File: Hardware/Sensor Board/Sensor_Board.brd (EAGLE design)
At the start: 100 x 80 mm, 15 parts, among them U1 ATMEGA328P_PDIP

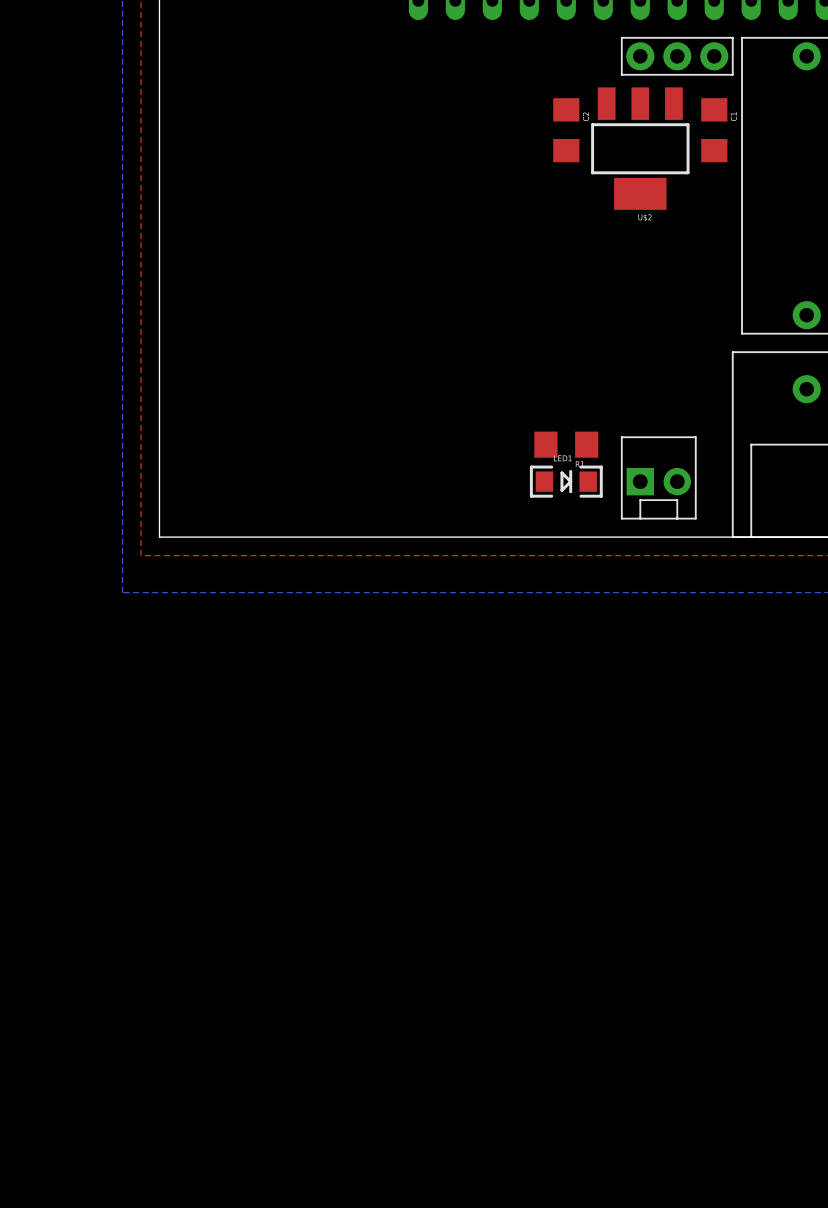
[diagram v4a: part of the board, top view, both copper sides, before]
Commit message: Reorganize Schematic
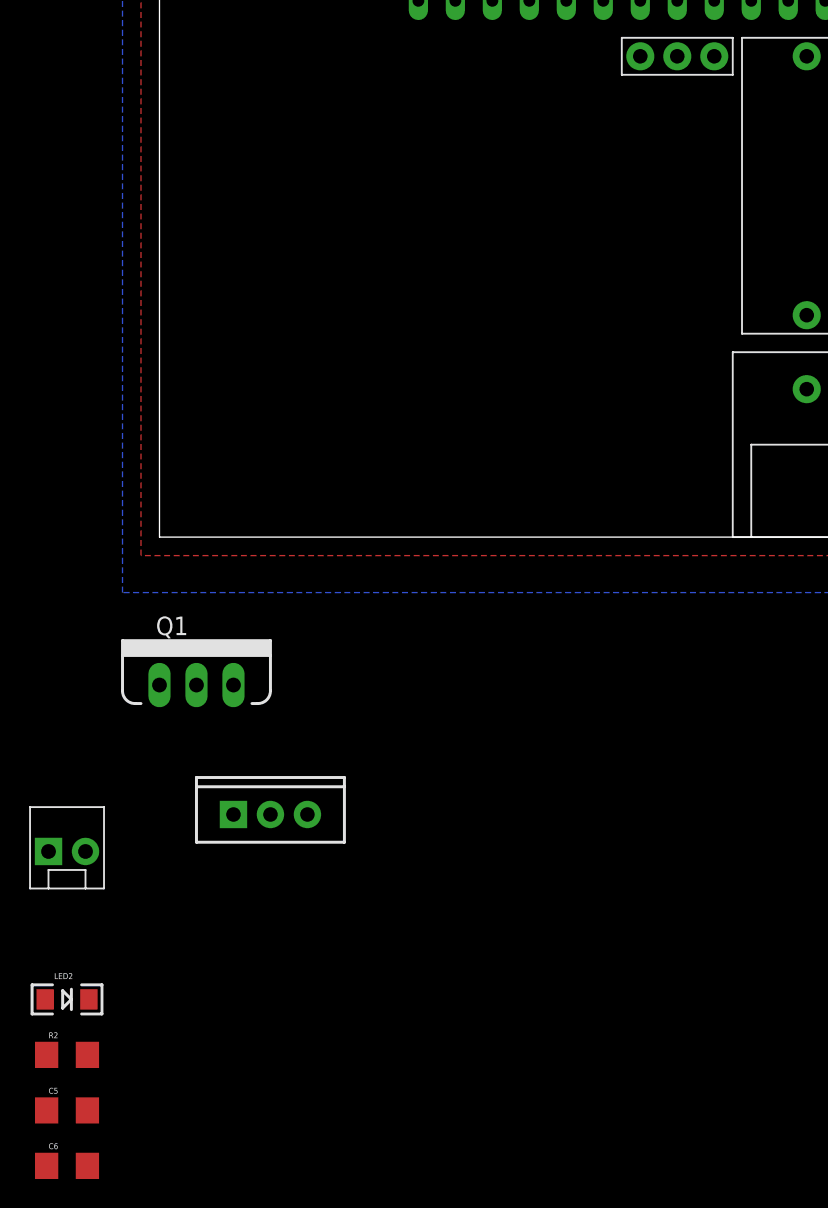
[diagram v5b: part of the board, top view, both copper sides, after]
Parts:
- removed C1, C2: .1uF, SparkFun-Passives:1206
- removed JP2: M02POLAR, SparkFun-Connectors:MOLEX-1X2
- removed LED1: (no value), SparkFun-LED:LED-1206
- removed R1: 1k, SparkFun-Passives:1206
- removed U$2: V_REG_LM3940, SparkFun-PowerIC:SOT223
- added C5: 100uF, SparkFun-Capacitors:1206
- added C6: 10uF, SparkFun-Capacitors:1206
- added IC1: (no value), SparkFun-PowerIC:TO220-IGO
- added JP1: M02POLAR, SparkFun-Connectors:MOLEX-1X2
- added LED2: (no value), SparkFun-LED:LED-1206
- added Q1: MOSFET-NCHANNELFQP30N06L, SparkFun-DiscreteSemi:TO220V
- added R2: 1k, SparkFun-Passives:1206
- C3, C4: value (none) -> 22pF
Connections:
- net RX renamed PH_SENS_RX
- net TO_LAZER renamed 3V3_LASER
- net TX renamed PH_SENS_TX
- removed net N$8: LED1.A, R1.2
- removed net TO_MOSFET: JP3.1
- new net 12V: C5.1, IC1.IN, JP1.2
- new net N$1: JP3.1, Q1.2
- new net N$3: LED2.C, R2.1
- net 3.3V: no longer C2.1, U$2.3
- net 5V: now also C6.1, IC1.OUT, LED2.A; no longer C1.1, JP2.2, R1.1, U$2.1
- net GND: now also C5.2, C6.2, IC1.GND, JP1.1, R2.2; no longer C1.2, C2.2, JP2.1, LED1.C, U$2.2
- net LASER_CTR: now also Q1.1
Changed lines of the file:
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@@
 </autorouter>
 <elements>
-<element name="JP2" library="SparkFun-Connectors" package="MOLEX-1X2" value="M02POLAR" x="33.02" y="3.81"/>
 <element name="JP3" library="SparkFun-Connectors" package="MOLEX-1X2" value="M02POLAR" x="16.51" y="49.53" rot="R180"/>
-<element name="U$2" library="SparkFun-PowerIC" package="SOT223" value="V_REG_LM3940" x="33.02" y="26.67" rot="R180"/>
-<element name="C1" library="SparkFun-Passives" package="1206" value=".1uF" x="38.1" y="27.94" rot="R270"/>
-<element name="C2" library="SparkFun-Passives" package="1206" value=".1uF" x="27.94" y="27.94" rot="R270"/>
-<element name="LED1" library="SparkFun-LED" package="LED-1206" value="" x="27.94" y="3.81"/>
-<element name="R1" library="SparkFun-Passives" package="1206" value="1k" x="27.94" y="6.35" rot="R180"/>
 <element name="U$3" library="pH_EZ0" package="PH_EZ0" value="PH_EZ0" x="40.005" y="13.97"/>
 <element name="U$4" library="PH_CONNECTOR" package="PH_CONNECTOR" value="PH_CONNECTOR" x="46.99" y="7.62"/>
@@
 <element name="U1" library="SparkFun-DigitalIC" package="DIL28-3" value="ATMEGA328P_PDIP" x="34.29" y="40.64" rot="R180"/>
 <element name="U$5" library="moisture sensor" package="MOISTURE_SENSOR" value="MOISTURE_SENSOR" x="35.56" y="33.02"/>
-<element name="C3" library="SparkFun-Passives" package="1206" value="" x="29.21" y="46.99"/>
-<element name="C4" library="SparkFun-Passives" package="1206" value="" x="22.86" y="46.99" rot="R180"/>
+<element name="C3" library="SparkFun-Passives" package="1206" value="22pF" x="29.21" y="46.99"/>
+<element name="C4" library="SparkFun-Passives" package="1206" value="22pF" x="22.86" y="46.99" rot="R180"/>
 <element name="U$6" library="CCD_CONNECTOR" package="CCD_CONNECTOR" value="CCD_CONNECTOR" x="38.1" y="48.26" rot="R180"/>
+<element name="Q1" library="SparkFun-DiscreteSemi" package="TO220V" value="MOSFET-NCHANNELFQP30N06L" x="2.54" y="-10.16">
+<attribute name="PROD_ID" value="TRANS-10060" x="2.54" y="-10.16" size="1.778" layer="27" display="off"/>
+</element>
+<element name="IC1" library="SparkFun-PowerIC" package="TO220-IGO" value="" x="7.62" y="-19.05"/>
+<element name="JP1" library="SparkFun-Connectors" package="MOLEX-1X2" value="M02POLAR" x="-7.62" y="-21.59"/>
+<element name="LED2" library="SparkFun-LED" package="LED-1206" value="" x="-6.35" y="-31.75"/>
+<element name="R2" library="SparkFun-Passives" package="1206" value="1k" x="-6.35" y="-35.56"/>
+<element name="C5" library="SparkFun-Capacitors" package="1206" value="100uF" x="-6.35" y="-39.37"/>
+<element name="C6" library="SparkFun-Capacitors" package="1206" value="10uF" x="-6.35" y="-43.18"/>
 </elements>
 <signals>
 <signal name="GND">
-<contactref element="JP2" pad="1"/>
-<contactref element="C1" pad="2"/>
-<contactref element="U$2" pad="2"/>
-<contactref element="C2" pad="2"/>
-<contactref element="LED1" pad="C"/>
 <contactref element="U$3" pad="GND"/>
-<contactref element="U$3" pad="PGND"/>
-<contactref element="U$4" pad="GND"/>
 <contactref element="U1" pad="22"/>
 <contactref element="U1" pad="8"/>
@@
 <contactref element="C3" pad="2"/>
 <contactref element="U$6" pad="GND"/>
+<contactref element="IC1" pad="GND"/>
+<contactref element="JP1" pad="1"/>
+<contactref element="R2" pad="2"/>
+<contactref element="C5" pad="2"/>
+<contactref element="C6" pad="2"/>
+<contactref element="U$3" pad="PGND"/>
+<contactref element="U$4" pad="GND"/>
 <wire x1="33.02" y1="44.45" x2="30.61" y2="46.99" width="0" layer="19" extent="1-1"/>
-<wire x1="33.02" y1="29.7688" x2="33.02" y2="33.02" width="0" layer="19" extent="1-1"/>
-<wire x1="29.44" y1="3.81" x2="33.02" y2="3.81" width="0" layer="19" extent="1-1"/>
-<wire x1="38.1" y1="26.54" x2="33.02" y2="29.7688" width="0" layer="19" extent="1-1"/>
-<wire x1="27.94" y1="26.54" x2="33.02" y2="29.7688" width="0" layer="19" extent="1-1"/>
 <wire x1="21.46" y1="46.99" x2="30.61" y2="46.99" width="0" layer="19" extent="1-1"/>
+<wire x1="7.62" y1="-19.05" x2="49.53" y2="10.16" width="0" layer="19" extent="1-1"/>
+<wire x1="-7.62" y1="-21.59" x2="7.62" y2="-19.05" width="0" layer="19" extent="1-1"/>
+<wire x1="-4.95" y1="-35.56" x2="-7.62" y2="-21.59" width="0" layer="19" extent="1-1"/>
+<wire x1="-4.95" y1="-39.37" x2="-4.95" y2="-35.56" width="0" layer="19" extent="1-1"/>
+<wire x1="-4.95" y1="-43.18" x2="-4.95" y2="-39.37" width="0" layer="19" extent="1-1"/>
 </signal>
 <signal name="5V">
-<contactref element="JP2" pad="2"/>
-<contactref element="U$2" pad="1"/>
-<contactref element="C1" pad="1"/>
-<contactref element="R1" pad="1"/>
-<contactref element="U$3" pad="VCC"/>
-<contactref element="U$4" pad="VCC"/>
 <contactref element="U$5" pad="VCC"/>
 <polygon width="0.4064" layer="1">
@@
 </polygon>
 <contactref element="U$6" pad="5V"/>
+<contactref element="IC1" pad="OUT"/>
+<contactref element="LED2" pad="A"/>
+<contactref element="C6" pad="1"/>
+<contactref element="U$3" pad="VCC"/>
+<contactref element="U$4" pad="VCC"/>
+<wire x1="-7.85" y1="-31.75" x2="-7.75" y2="-43.18" width="0" layer="19" extent="1-1"/>
+<wire x1="10.16" y1="-19.05" x2="-7.85" y2="-31.75" width="0" layer="19" extent="1-1"/>
+<wire x1="44.45" y1="10.16" x2="10.16" y2="-19.05" width="0" layer="19" extent="1-1"/>
 </signal>
 <signal name="3.3V">
-<contactref element="C2" pad="1"/>
-<contactref element="U$2" pad="3"/>
 <contactref element="U1" pad="7"/>
 <contactref element="U1" pad="21"/>
@@
 <wire x1="33.02" y1="36.83" x2="35.56" y2="44.45" width="0" layer="19" extent="1-1"/>
 <wire x1="30.48" y1="36.83" x2="33.02" y2="36.83" width="0" layer="19" extent="1-1"/>
-<wire x1="30.7086" y1="29.7688" x2="30.48" y2="36.83" width="0" layer="19" extent="1-1"/>
-<wire x1="27.94" y1="29.34" x2="30.7086" y2="29.7688" width="0" layer="19" extent="1-1"/>
-</signal>
-<signal name="N$8">
-<contactref element="R1" pad="2"/>
-<contactref element="LED1" pad="A"/>
-<wire x1="26.44" y1="3.81" x2="26.54" y2="6.35" width="0" layer="19" extent="1-1"/>
-</signal>
-<signal name="RX">
-<contactref element="U$3" pad="RX"/>
-<contactref element="U1" pad="4"/>
-<wire x1="49.53" y1="33.02" x2="43.18" y2="44.45" width="0" layer="19" extent="1-1"/>
 </signal>
 <signal name="N$5">
@@
 <wire x1="24.26" y1="46.99" x2="22.86" y2="50.8" width="0" layer="19" extent="1-1"/>
 <wire x1="27.94" y1="44.45" x2="24.26" y2="46.99" width="0" layer="19" extent="1-1"/>
-</signal>
-<signal name="TX">
-<contactref element="U$3" pad="TX"/>
-<contactref element="U1" pad="5"/>
-<wire x1="46.99" y1="33.02" x2="40.64" y2="44.45" width="0" layer="19" extent="1-1"/>
 </signal>
 <signal name="MOIS_SENSOR">
@@
 <signal name="LASER_CTR">
 <contactref element="U1" pad="12"/>
+<contactref element="Q1" pad="1"/>
+<wire x1="0" y1="-10.16" x2="22.86" y2="44.45" width="0" layer="19" extent="1-1"/>
 </signal>
-<signal name="TO_LAZER">
+<signal name="3V3_LASER">
 <contactref element="JP3" pad="2"/>
-</signal>
-<signal name="TO_MOSFET">
-<contactref element="JP3" pad="1"/>
 </signal>
 <signal name="N$2">
@@
 <wire x1="30.48" y1="44.45" x2="27.81" y2="46.99" width="0" layer="19" extent="1-1"/>
 </signal>
+<signal name="N$1">
+<contactref element="JP3" pad="1"/>
+<contactref element="Q1" pad="2"/>
+<wire x1="2.54" y1="-10.16" x2="16.51" y2="49.53" width="0" layer="19" extent="1-1"/>
+</signal>
+<signal name="PH_SENS_RX">
+<contactref element="U1" pad="4"/>
+<contactref element="U$3" pad="RX"/>
+<wire x1="49.53" y1="33.02" x2="43.18" y2="44.45" width="0" layer="19" extent="1-1"/>
+</signal>
+<signal name="PH_SENS_TX">
+<contactref element="U1" pad="5"/>
+<contactref element="U$3" pad="TX"/>
+<wire x1="46.99" y1="33.02" x2="40.64" y2="44.45" width="0" layer="19" extent="1-1"/>
+</signal>
+<signal name="12V">
+<contactref element="JP1" pad="2"/>
+<contactref element="IC1" pad="IN"/>
+<contactref element="C5" pad="1"/>
+<wire x1="-5.08" y1="-21.59" x2="-7.75" y2="-39.37" width="0" layer="19" extent="1-1"/>
+<wire x1="5.08" y1="-19.05" x2="-5.08" y2="-21.59" width="0" layer="19" extent="1-1"/>
+</signal>
+<signal name="N$3">
+<contactref element="LED2" pad="C"/>
+<contactref element="R2" pad="1"/>
+<wire x1="-4.85" y1="-31.75" x2="-7.75" y2="-35.56" width="0" layer="19" extent="1-1"/>
+</signal>
 </signals>

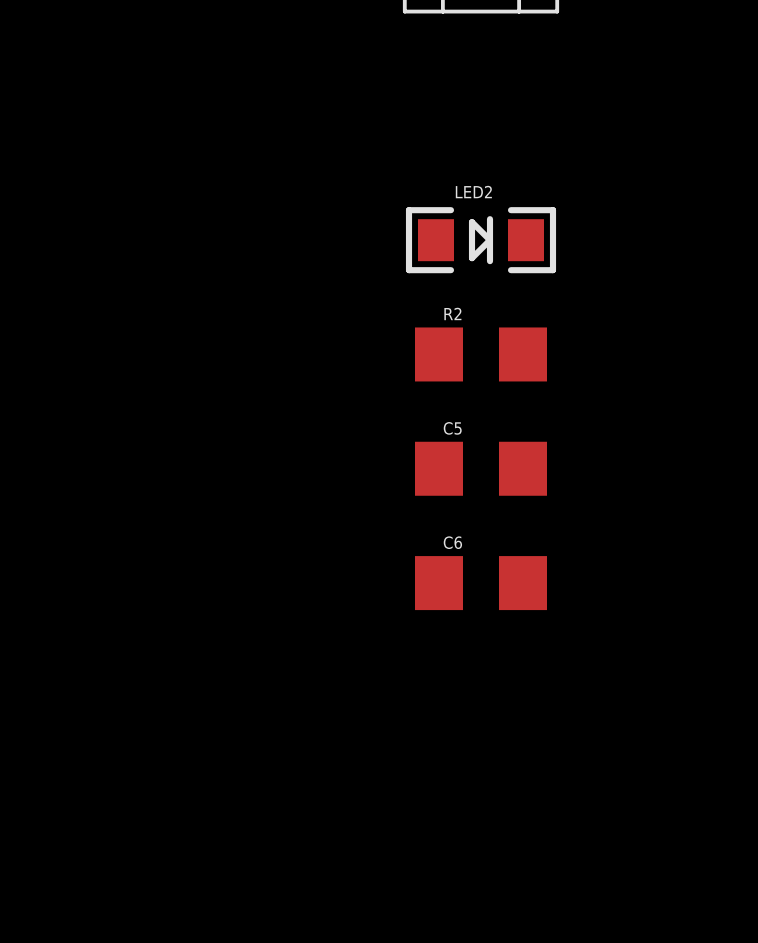
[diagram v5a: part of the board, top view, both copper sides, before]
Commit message: Complete laser power system
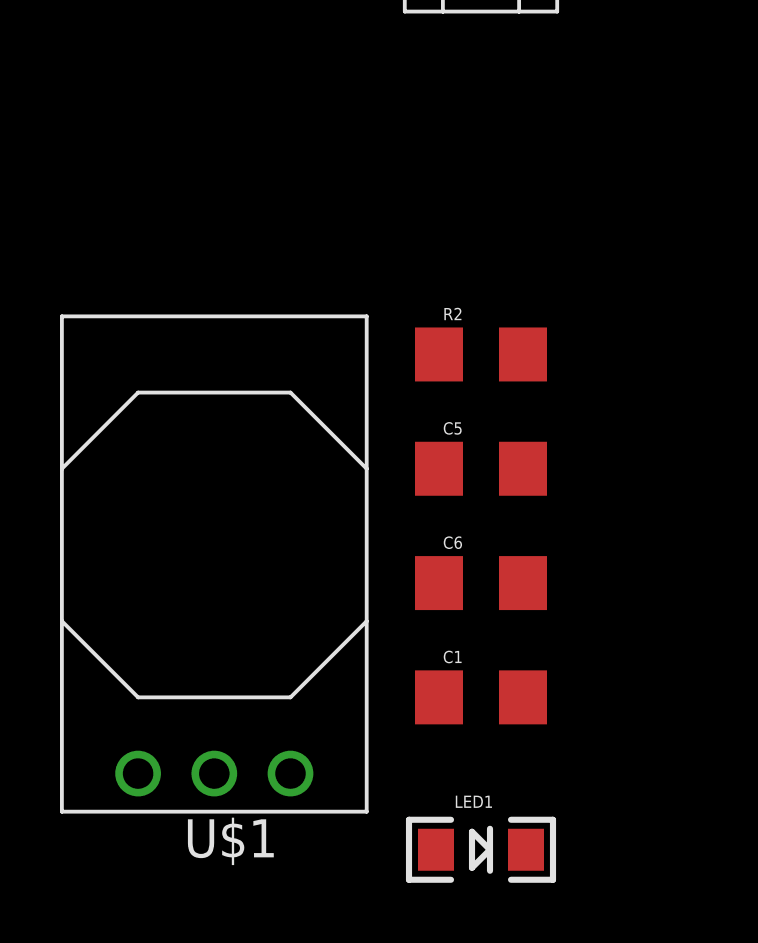
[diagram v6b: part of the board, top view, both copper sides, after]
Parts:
- removed LED2: (no value), SparkFun-LED:LED-1206
- added C1: 100uF, SparkFun-Capacitors:1206
- added LED1: (no value), SparkFun-LED:LED-1206
- added U$1: Q_OKI-78SR, MRDT-2015-PowerBoard:OKI-78SRH
- added U$2: TEST, MRDT-2015-General:TEST
- renumbered IC1 to LM7805, JP1 to 12V_INPUT
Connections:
- net 12V: now also U$1.1
- net 3V3_LASER: now also C1.1, U$1.3
- net 5V: now also LED1.A; no longer LED2.A
- net GND: now also C1.2, Q1.3, U$1.2
- net N$3: now also LED1.C; no longer LED2.C
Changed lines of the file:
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@@
 <attribute name="PROD_ID" value="TRANS-10060" x="2.54" y="-10.16" size="1.778" layer="27" display="off"/>
 </element>
-<element name="IC1" library="SparkFun-PowerIC" package="TO220-IGO" value="" x="7.62" y="-19.05"/>
-<element name="JP1" library="SparkFun-Connectors" package="MOLEX-1X2" value="M02POLAR" x="-7.62" y="-21.59"/>
-<element name="LED2" library="SparkFun-LED" package="LED-1206" value="" x="-6.35" y="-31.75"/>
+<element name="LM7805" library="SparkFun-PowerIC" package="TO220-IGO" value="" x="7.62" y="-19.05"/>
+<element name="12V_INPUT" library="SparkFun-Connectors" package="MOLEX-1X2" value="M02POLAR" x="-7.62" y="-21.59"/>
 <element name="R2" library="SparkFun-Passives" package="1206" value="1k" x="-6.35" y="-35.56"/>
 <element name="C5" library="SparkFun-Capacitors" package="1206" value="100uF" x="-6.35" y="-39.37"/>
 <element name="C6" library="SparkFun-Capacitors" package="1206" value="10uF" x="-6.35" y="-43.18"/>
+<element name="C1" library="SparkFun-Capacitors" package="1206" value="100uF" x="-6.35" y="-46.99"/>
+<element name="LED1" library="SparkFun-LED" package="LED-1206" value="" x="-6.35" y="-52.07"/>
+<element name="U$1" library="MRDT-2015-PowerBoard" package="OKI-78SRH" value="Q_OKI-78SR" x="-15.24" y="-49.53"/>
+<element name="U$2" library="MRDT-2015-General" package="TEST" value="TEST" x="6.35" y="-104.14"/>
 </elements>
 <signals>
@@
 <contactref element="C3" pad="2"/>
 <contactref element="U$6" pad="GND"/>
-<contactref element="IC1" pad="GND"/>
-<contactref element="JP1" pad="1"/>
+<contactref element="LM7805" pad="GND"/>
+<contactref element="12V_INPUT" pad="1"/>
 <contactref element="R2" pad="2"/>
 <contactref element="C5" pad="2"/>
@@
 <contactref element="U$3" pad="PGND"/>
 <contactref element="U$4" pad="GND"/>
+<contactref element="Q1" pad="3"/>
+<contactref element="C1" pad="2"/>
+<contactref element="U$1" pad="2"/>
 <wire x1="33.02" y1="44.45" x2="30.61" y2="46.99" width="0" layer="19" extent="1-1"/>
 <wire x1="21.46" y1="46.99" x2="30.61" y2="46.99" width="0" layer="19" extent="1-1"/>
-<wire x1="7.62" y1="-19.05" x2="49.53" y2="10.16" width="0" layer="19" extent="1-1"/>
+<wire x1="5.08" y1="-10.16" x2="49.53" y2="10.16" width="0" layer="19" extent="1-1"/>
+<wire x1="7.62" y1="-19.05" x2="5.08" y2="-10.16" width="0" layer="19" extent="1-1"/>
 <wire x1="-7.62" y1="-21.59" x2="7.62" y2="-19.05" width="0" layer="19" extent="1-1"/>
 <wire x1="-4.95" y1="-35.56" x2="-7.62" y2="-21.59" width="0" layer="19" extent="1-1"/>
 <wire x1="-4.95" y1="-39.37" x2="-4.95" y2="-35.56" width="0" layer="19" extent="1-1"/>
 <wire x1="-4.95" y1="-43.18" x2="-4.95" y2="-39.37" width="0" layer="19" extent="1-1"/>
+<wire x1="-4.95" y1="-46.99" x2="-4.95" y2="-43.18" width="0" layer="19" extent="1-1"/>
+<wire x1="-15.24" y1="-49.53" x2="-4.95" y2="-46.99" width="0" layer="19" extent="1-1"/>
 </signal>
 <signal name="5V">
@@
 </polygon>
 <contactref element="U$6" pad="5V"/>
-<contactref element="IC1" pad="OUT"/>
-<contactref element="LED2" pad="A"/>
+<contactref element="LM7805" pad="OUT"/>
 <contactref element="C6" pad="1"/>
 <contactref element="U$3" pad="VCC"/>
 <contactref element="U$4" pad="VCC"/>
-<wire x1="-7.85" y1="-31.75" x2="-7.75" y2="-43.18" width="0" layer="19" extent="1-1"/>
-<wire x1="10.16" y1="-19.05" x2="-7.85" y2="-31.75" width="0" layer="19" extent="1-1"/>
+<contactref element="LED1" pad="A"/>
+<wire x1="-7.75" y1="-43.18" x2="-7.85" y2="-52.07" width="0" layer="19" extent="1-1"/>
+<wire x1="10.16" y1="-19.05" x2="-7.75" y2="-43.18" width="0" layer="19" extent="1-1"/>
 <wire x1="44.45" y1="10.16" x2="10.16" y2="-19.05" width="0" layer="19" extent="1-1"/>
 </signal>
@@
 <signal name="3V3_LASER">
 <contactref element="JP3" pad="2"/>
+<contactref element="C1" pad="1"/>
+<contactref element="U$1" pad="3"/>
+<wire x1="-7.75" y1="-46.99" x2="-17.78" y2="-49.53" width="0" layer="19" extent="1-1"/>
+<wire x1="13.97" y1="49.53" x2="-7.75" y2="-46.99" width="0" layer="19" extent="1-1"/>
 </signal>
 <signal name="N$2">
@@
 </signal>
 <signal name="12V">
-<contactref element="JP1" pad="2"/>
-<contactref element="IC1" pad="IN"/>
+<contactref element="12V_INPUT" pad="2"/>
+<contactref element="LM7805" pad="IN"/>
 <contactref element="C5" pad="1"/>
+<contactref element="U$1" pad="1"/>
+<wire x1="-7.75" y1="-39.37" x2="-12.7" y2="-49.53" width="0" layer="19" extent="1-1"/>
 <wire x1="-5.08" y1="-21.59" x2="-7.75" y2="-39.37" width="0" layer="19" extent="1-1"/>
 <wire x1="5.08" y1="-19.05" x2="-5.08" y2="-21.59" width="0" layer="19" extent="1-1"/>
 </signal>
 <signal name="N$3">
-<contactref element="LED2" pad="C"/>
+<contactref element="LED1" pad="C"/>
 <contactref element="R2" pad="1"/>
-<wire x1="-4.85" y1="-31.75" x2="-7.75" y2="-35.56" width="0" layer="19" extent="1-1"/>
+<wire x1="-7.75" y1="-35.56" x2="-4.85" y2="-52.07" width="0" layer="19" extent="1-1"/>
 </signal>
 </signals>
